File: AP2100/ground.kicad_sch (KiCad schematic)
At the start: 9 parts, among them U7 LS1043ASE7xxx

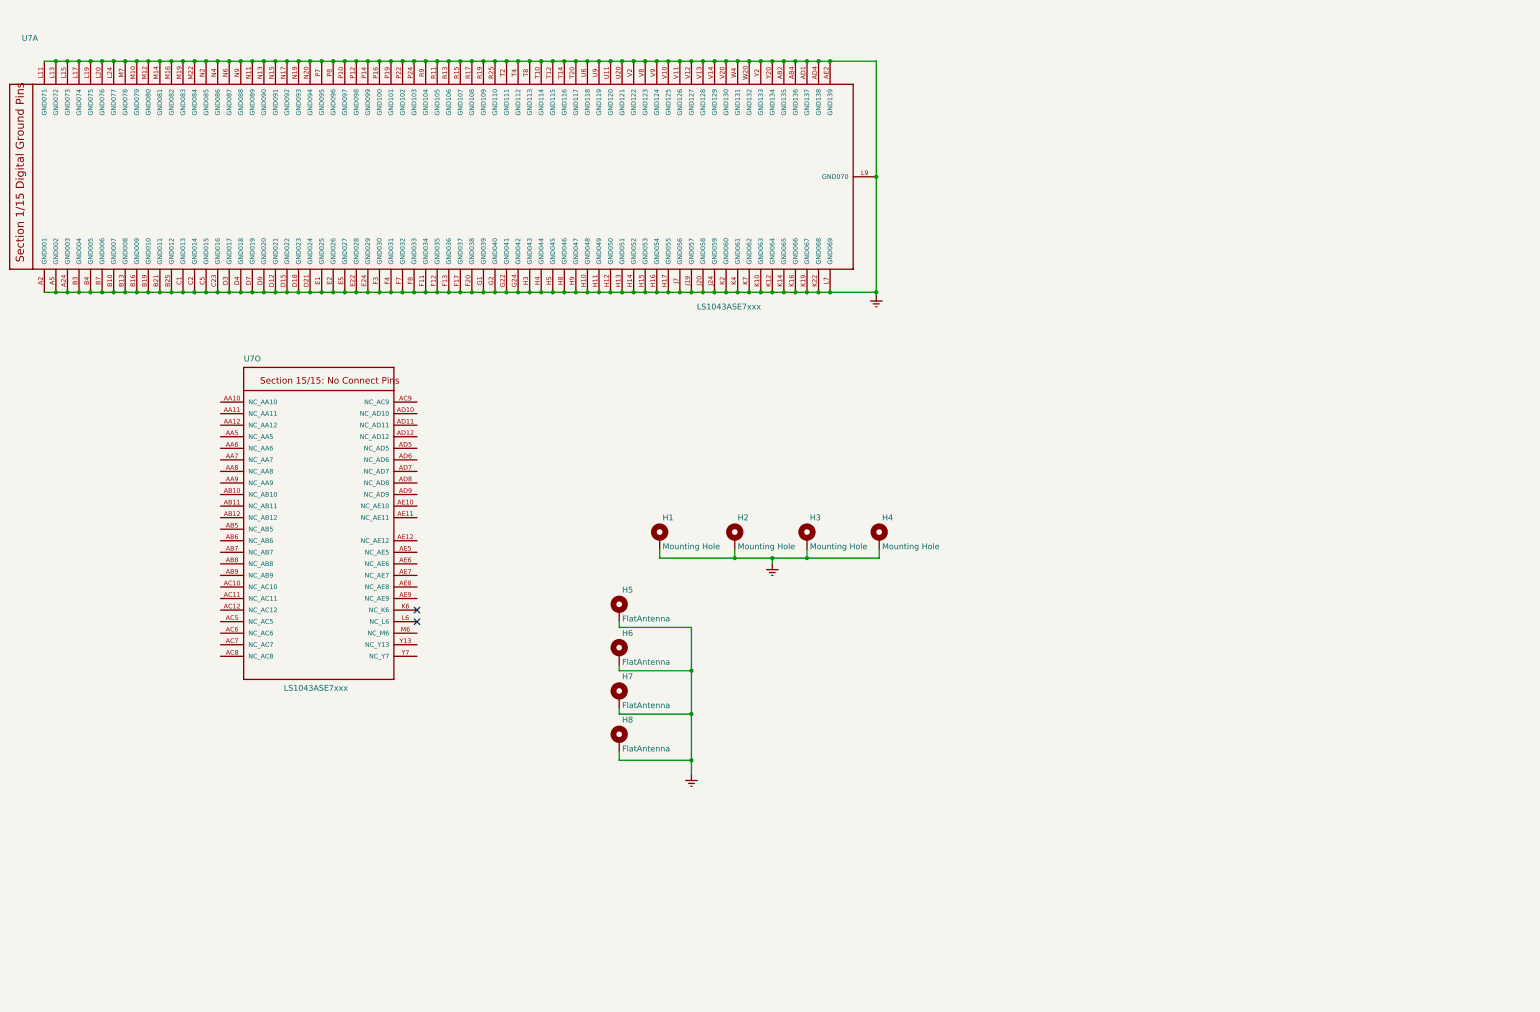
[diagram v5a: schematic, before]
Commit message: More cleanups - fix incorrect serial console pinout Add netclasses
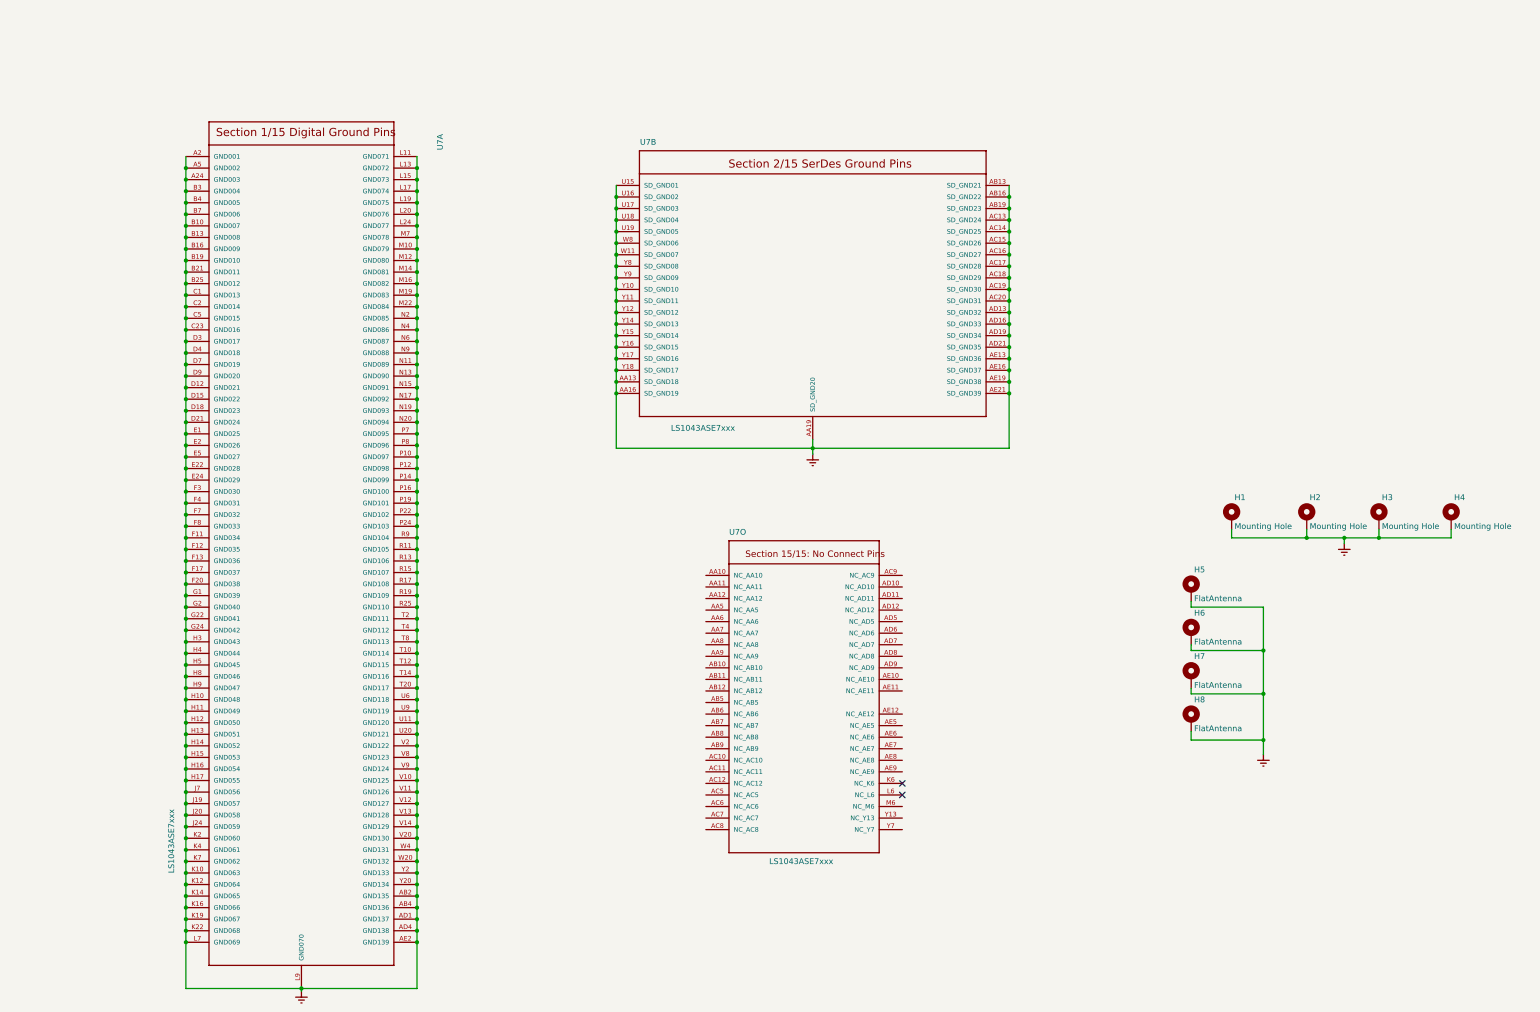
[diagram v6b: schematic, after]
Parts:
- added unit 2 of U7
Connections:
- net GND: now also U7.AA13 (SD_GND18), U7.AA16 (SD_GND19), U7.AA19 (SD_GND20), U7.AB13 (SD_GND21), U7.AB16 (SD_GND22), U7.AB19 (SD_GND23), U7.AC13 (SD_GND24), U7.AC14 (SD_GND25), U7.AC15 (SD_GND26), U7.AC16 (SD_GND27), U7.AC17 (SD_GND28), U7.AC18 (SD_GND29), U7.AC19 (SD_GND30), U7.AC20 (SD_GND31), U7.AD13 (SD_GND32), U7.AD16 (SD_GND33), U7.AD19 (SD_GND34), U7.AD21 (SD_GND35), U7.AE13 (SD_GND36), U7.AE16 (SD_GND37), U7.AE19 (SD_GND38), U7.AE21 (SD_GND39), U7.U15 (SD_GND01), U7.U16 (SD_GND02), U7.U17 (SD_GND03), U7.U18 (SD_GND04), U7.U19 (SD_GND05), U7.W11 (SD_GND07), U7.W8 (SD_GND06), U7.Y10 (SD_GND10), U7.Y11 (SD_GND11), U7.Y12 (SD_GND12), U7.Y14 (SD_GND13), U7.Y15 (SD_GND14), U7.Y16 (SD_GND15), U7.Y17 (SD_GND16), U7.Y18 (SD_GND17), U7.Y8 (SD_GND08), U7.Y9 (SD_GND09)
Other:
- company: (none) -> ISis ImageStream Internet Solutions, Inc.
- title: (none) -> AP2100
- moved on the sheet: H1, H2, H3, H4, H5, H6, H7, H8, U7A, U7O
